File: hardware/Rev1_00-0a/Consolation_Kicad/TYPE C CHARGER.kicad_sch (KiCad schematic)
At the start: 31 parts, among them J10 61300311121, J4 12401598E4#2A, J5 S2B-PH-K-S, U1 BQ25640VDLR

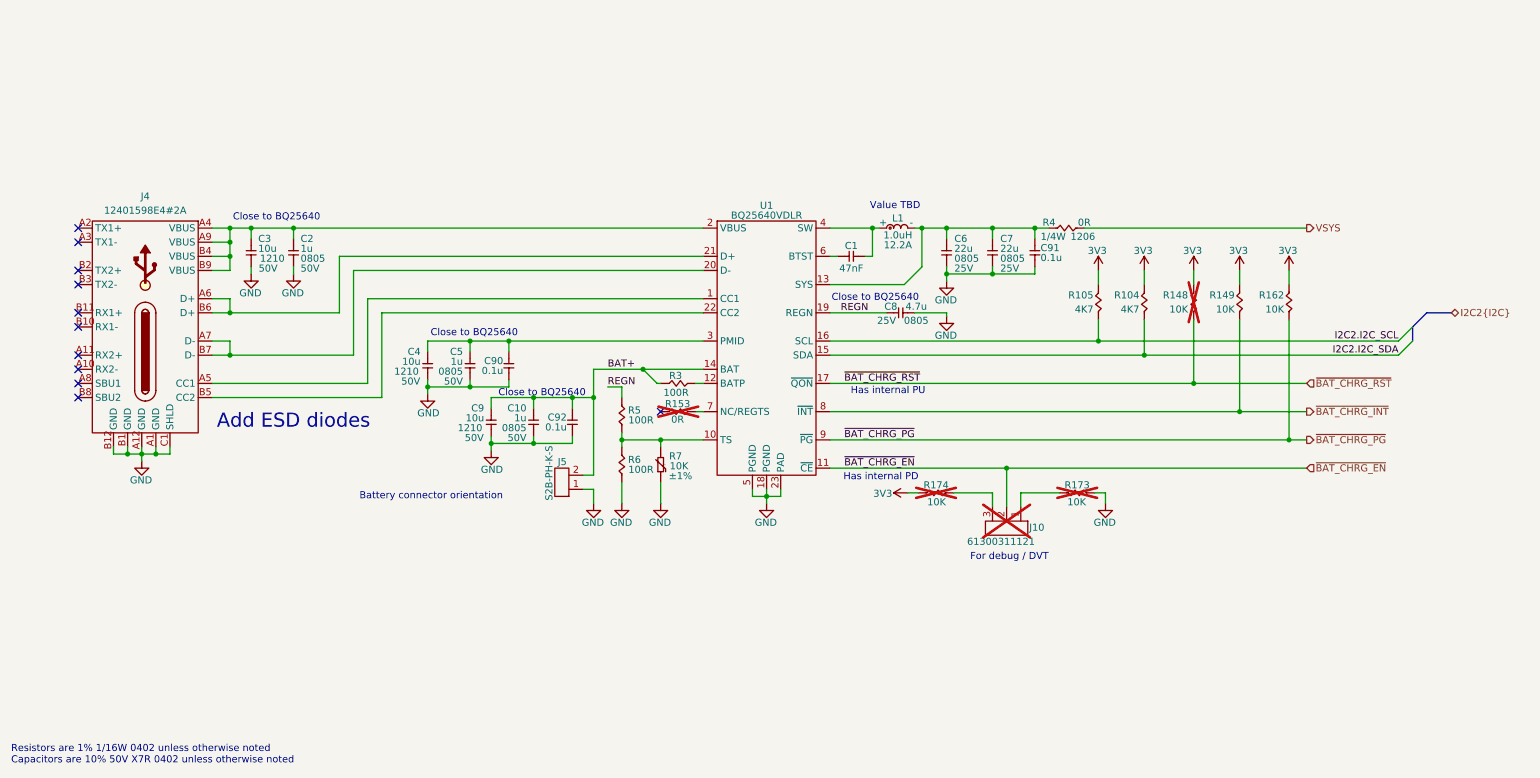
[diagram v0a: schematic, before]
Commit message: Removed unnecessary functions (USB2 mux, CapTouch) Adjusted 220uF alum capacitor for codec (slimmer version)
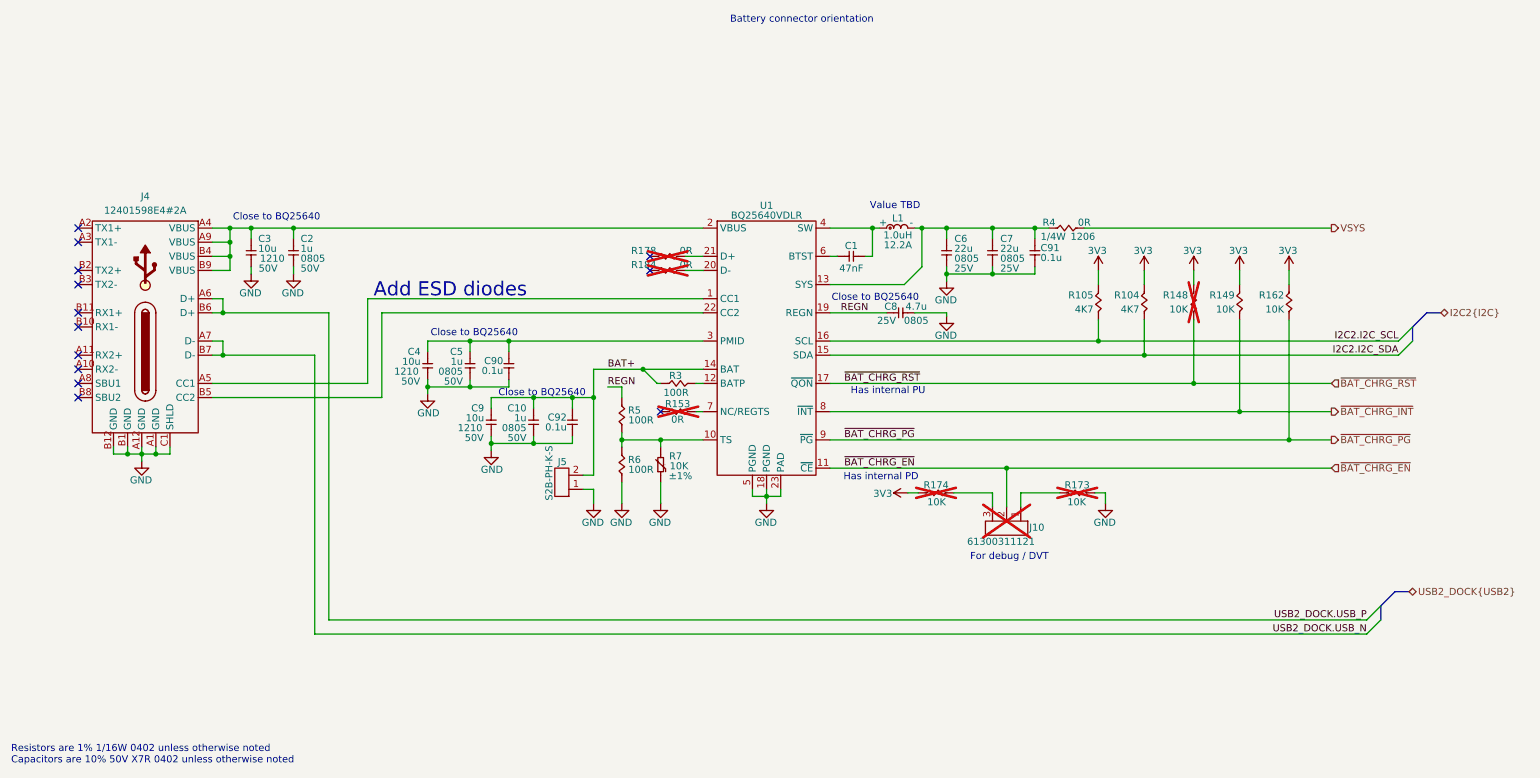
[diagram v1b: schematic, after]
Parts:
- added R178, R184: 0R, footprint:RES_0402, symbol KicadCompDb:Resistors/RES_SMT_00001
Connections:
- net USB2_DOCK.USB_P: now reaches J4.A6 (D+), J4.B6 (D+)
- net USB2_DOCK.USB_P: no longer U1.21 (D+)
- net USB2_DOCK.USB_N: now reaches J4.A7 (D-), J4.B7 (D-)
- net USB2_DOCK.USB_N: no longer U1.20 (D-)
- new net: R184.2, U1.20 (D-)
- new net: R178.2, U1.21 (D+)
- no-connect marks 11 -> 13

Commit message: Preliminary placement of Consolation continues
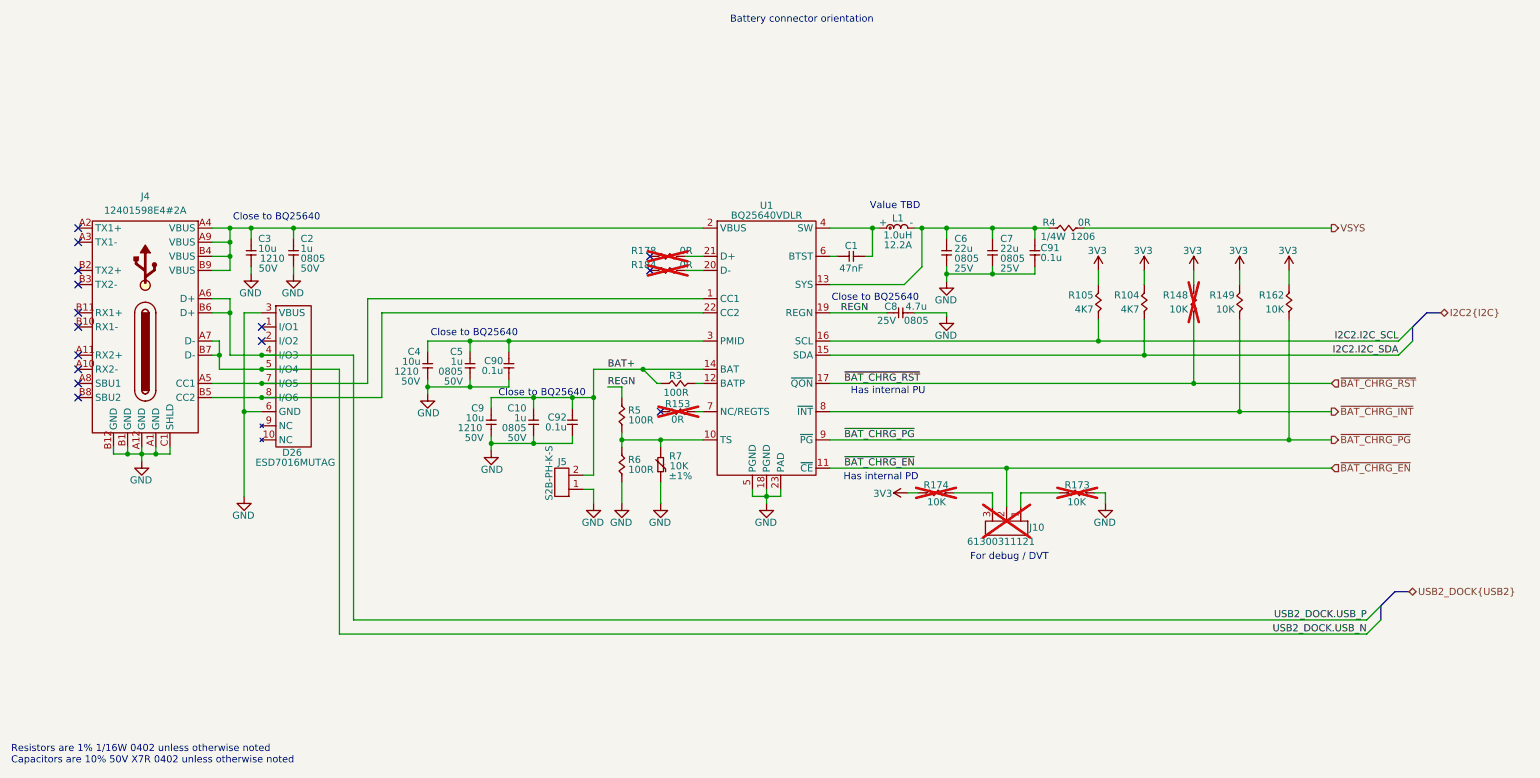
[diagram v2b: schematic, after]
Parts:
- added D26: ESD7016MUTAG, footprint:UDFN8, symbol KicadCompDb:ESD Diodes/ESD_DIODE_00001
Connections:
- net GND: now also D26.3 (VBUS), D26.6 (GND)
- net USB2_DOCK.USB_N: now also D26.5 (I/O4)
- net USB2_DOCK.USB_P: now also D26.4 (I/O3)
- net at J4.A5 (CC1), U1.1 (CC1): now also D26.7 (I/O5)
- net at J4.B5 (CC2), U1.22 (CC2): now also D26.8 (I/O6)
- no-connect marks 13 -> 15
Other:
- note removed: "Add ESD diodes"

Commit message: Work on preliminary placement + RP2350A fanout
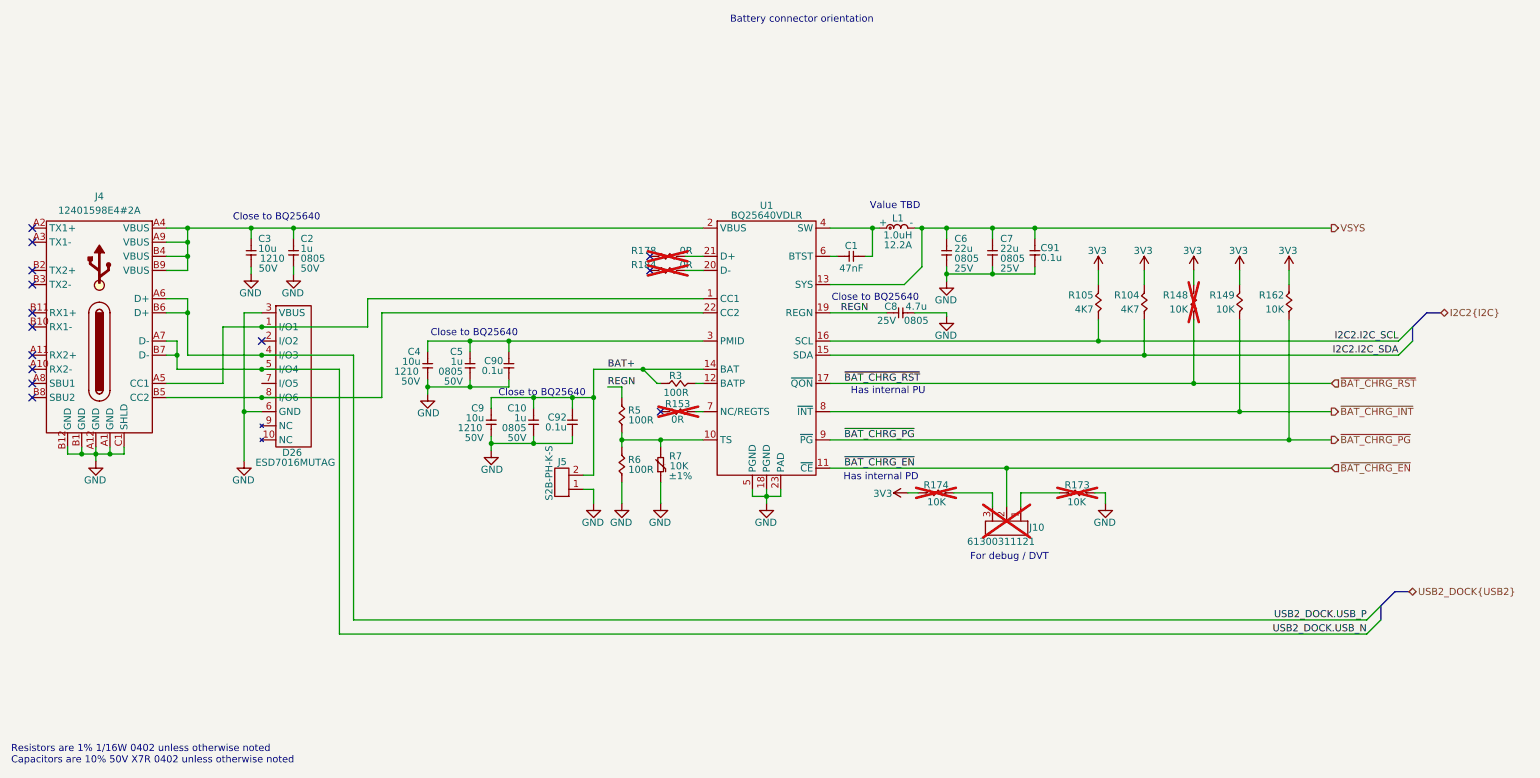
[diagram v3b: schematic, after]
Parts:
- removed R4: 0R, footprint:RES_1206, symbol KicadCompDb:Resistors/RES_SMT_00022
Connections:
- net VSYS: now also C6.2, C7.2, C91.2, L1.2 (-), U1.13 (SYS)
- net at J4.A5 (CC1), U1.1 (CC1): now also D26.1 (I/O1); no longer D26.7 (I/O5)
- no-connect marks 15 -> 14
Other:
- moved on the sheet: J4

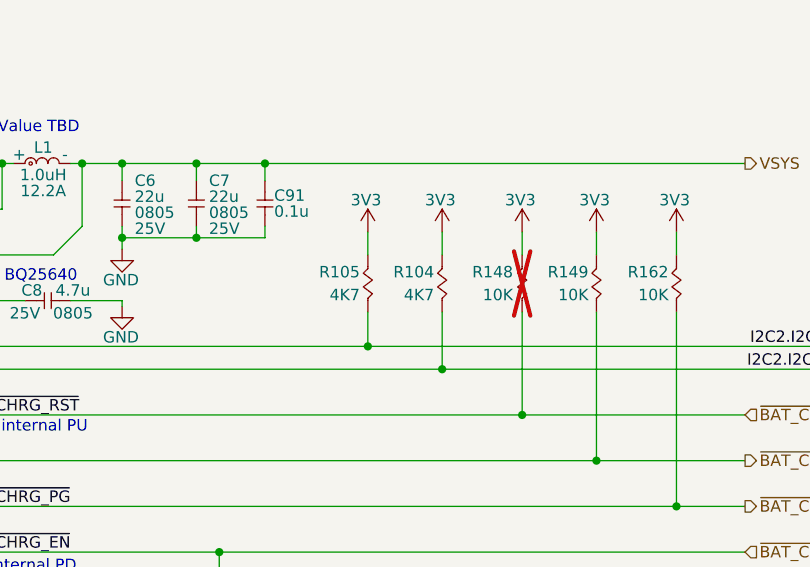
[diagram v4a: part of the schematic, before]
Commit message: Continue preliminary placement To do : Power supplies + Type C charger
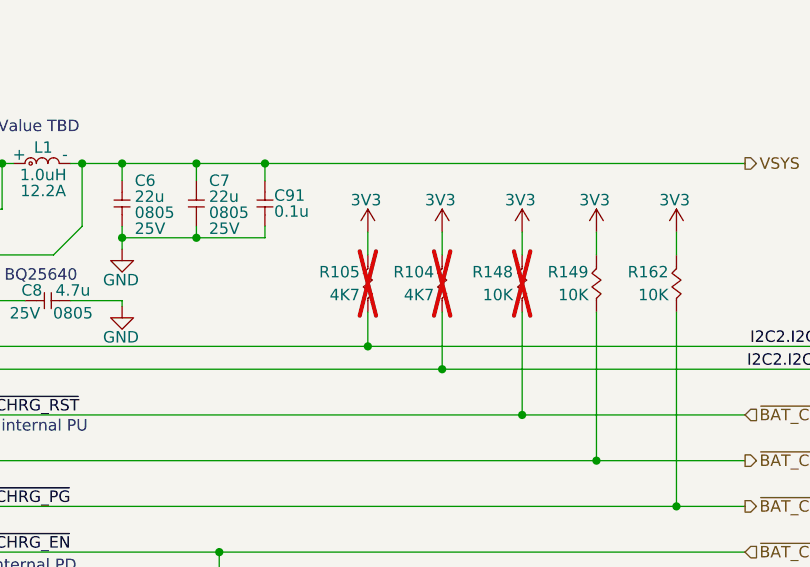
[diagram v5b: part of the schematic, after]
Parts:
- R104, R105: now not fitted
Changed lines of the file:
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@@
 	(title_block
 		(title "Consolation [Console Emulation]")
-		(date "2026-08-23")
+		(date "2026-08-29")
 		(rev "1.00-0A")
 		(comment 1 "Jean-Francois Bilodeau")
@@
 		(on_board yes)
 		(in_pos_files yes)
-		(dnp no)
+		(dnp yes)
 		(property "Reference" "R104"
 			(at 215.646 88.265 90)
@@
 		(on_board yes)
 		(in_pos_files yes)
-		(dnp no)
+		(dnp yes)
 		(property "Reference" "R105"
 			(at 207.391 88.265 90)

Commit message: Preliminary placement done Add test points to PCB
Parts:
- removed C91: 0.1u, footprint:CAP_NONPOL_0402, symbol KicadCompDb:Capacitors/CAP_CER_SMT_00001
- removed R178, R184: 0R, footprint:RES_0402, symbol KicadCompDb:Resistors/RES_SMT_00001
- added C13: 22u, footprint:CAP_NONPOL_0805, symbol KicadCompDb:Capacitors/CAP_CER_SMT_00011
- added D29: SMAJ20A, footprint:DO-214AC, symbol KicadCompDb:Diodes/DIODE_00009
- added TP37, TP38, TP39, TP40, TP41, TP42, TP43, TP44, TP49: 75 mils, footprint:SMT_TP_75_MILS, symbol KicadCompDb:Test Point/TP_00004
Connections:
- net BAT+: now also TP38.1
- net GND: now also C13.1, D29.2 (A)
- net VSYS: now also C13.2, TP44.1
- net ~{BAT_CHRG_INT}: now also TP42.1
- net ~{BAT_CHRG_PG}: now also TP41.1
- net ~{BAT_CHRG_RST}: now also TP43.1
- net at C2.2, C3.2, J4.A4 (VBUS)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: now also D29.1 (K), TP37.1
- net at D26.1 (I/O1), J4.A5 (CC1), U1.1 (CC1): now also TP39.1
- net at D26.8 (I/O6), J4.B5 (CC2), U1.22 (CC2): now also TP40.1
- net at R5.1, R6.2, R7.2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: now also TP49.1
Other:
- moved on the sheet: C2, C3

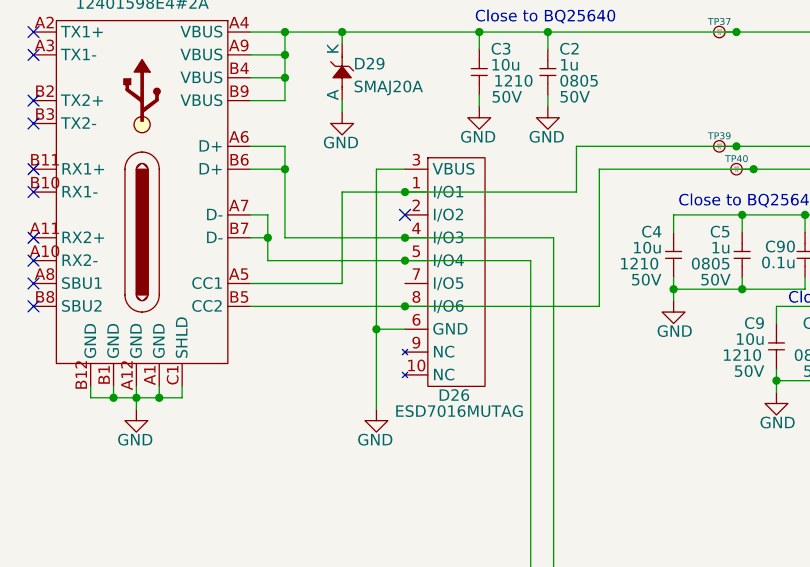
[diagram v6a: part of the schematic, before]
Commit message: Preliminary routing (DiffPairs, Power planes) in progress Slight changes to schematics to accommodate routing
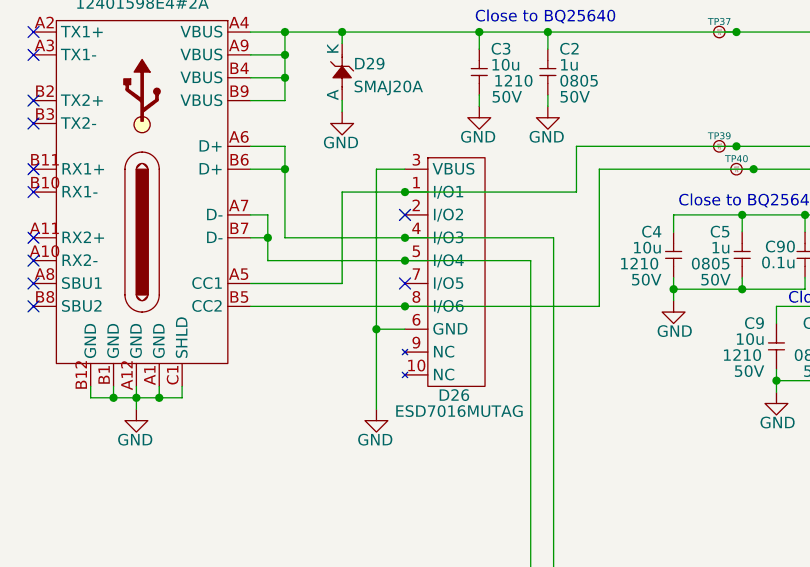
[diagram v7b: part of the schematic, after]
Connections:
- no-connect marks 14 -> 15
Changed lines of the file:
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@@
 	(title_block
 		(title "Consolation [Console Emulation]")
-		(date "2026-09-20")
+		(date "2026-10-12")
 		(rev "1.00-0A")
 		(comment 1 "Jean-Francois Bilodeau")
@@
 	(no_connect
 		(at 16.51 106.68)
+	)
+	(no_connect
+		(at 57.785 104.14)
 	)
 	(no_connect
@@
 			(justify right bottom)
 		)
-		(property "Net Class" "DP_90R"
+		(property "Netclass" "DP_90R"
 			(at 226.568 145.796 0)
 			(show_name no)
@@
 			(justify right bottom)
 		)
-		(property "Net Class" "DP_90R"
+		(property "Netclass" "DP_90R"
 			(at 226.568 148.336 0)
 			(show_name no)
